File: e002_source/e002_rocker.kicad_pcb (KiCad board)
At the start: 2 copper layers, 32.2 x 75.2 mm, 48 parts, among them IC1 IC_TEXAS_TPS62743YFPR, IC2 DRV8317HREER, J1 USB_C_Receptacle_USB2.0_16P, U1 ESP32-S3-WROOM-1-N8R2

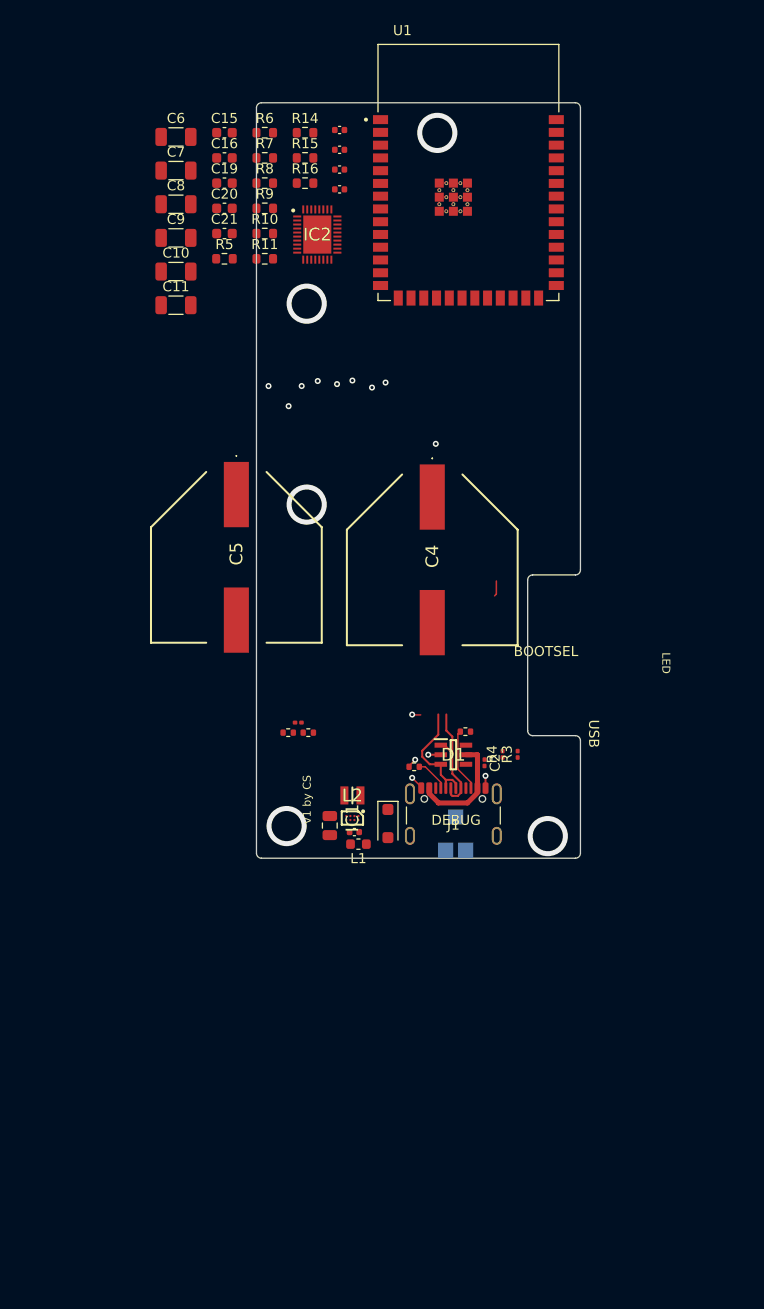
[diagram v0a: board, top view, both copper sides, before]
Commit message: removed STM MCU to optimize cost
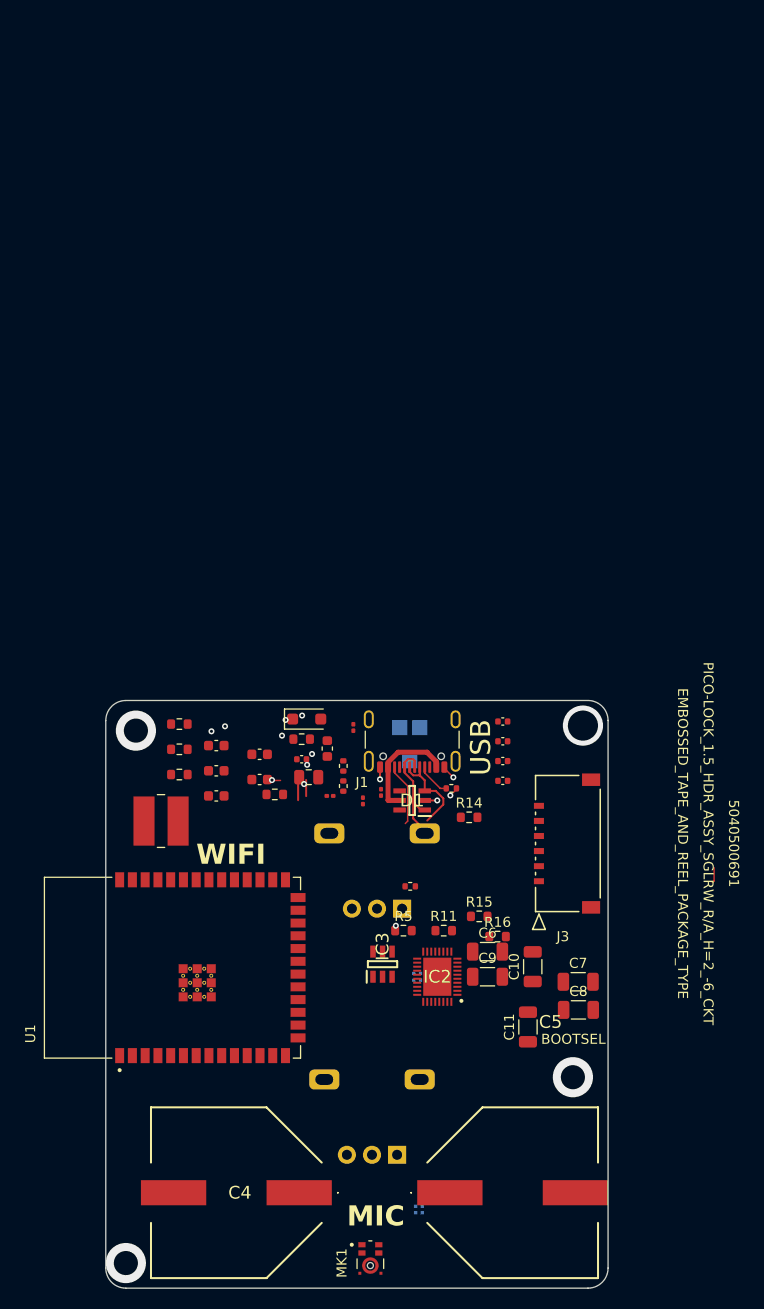
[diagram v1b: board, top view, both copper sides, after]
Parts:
- removed IC1: IC_TEXAS_TPS62743YFPR, smv_footprints:BGA8C40P2X4_87X156X53
- removed L2: 2.2u, smv_footprints:IND_MURATA_DFE201610P-2R2M=P2
- added IC3: ~, smv_footprints:SOT95P280X125-6N, F.Cu at (141.6, 127.8)
- added J3: 5040500691, smv_footprints:CONN_MOLEX_5040500691, F.Cu at (157.1, 119.5)
- added L3: INDC_TDK_VLCF5028T-220MR71-2, smv_footprints:IND_TDK_VLCF5028T-220MR71-2, F.Cu at (119.5, 113.5)
- added LED1: RGB, smv_footprints:DIOD_CREE_UHD111A-FKA-C3K23E1L3VG5ZB3Z3, B.Cu at (145.0, 129.0)
- added LED2: RGB, smv_footprints:DIOD_CREE_UHD111A-FKA-C3K23E1L3VG5ZB3Z3, B.Cu at (145.2, 152.2)
- added MK1: ~, smv_footprints:IC_MIC_TDK_MMICT5837-00-012, F.Cu at (140.3, 157.0)
- added RV1: R_Potentiometer, Potentiometer_THT:Potentiometer_Alps_RK09L_Single_Vertical, B.Cu at (143.0, 146.7)
- added RV1: R_Potentiometer, Potentiometer_THT:Potentiometer_Alps_RK09L_Single_Vertical, B.Cu at (143.5, 122.2)
- moved C7 90.1 mm to (161.0, 129.5)
- moved C8 89.7 mm to (161.1, 132.3)
- moved C6 86.8 mm to (152.0, 126.5)
- moved U1 84.5 mm to (120.6, 128.1), turned to 90 degrees
- moved C11 79.9 mm to (156.0, 134.0), turned to 90 degrees
- moved C9 79.8 mm to (152.0, 129.0)
- moved C10 77.8 mm to (156.5, 128.0), turned to 90 degrees
- moved R15 77.5 mm to (151.2, 123.0)
- moved R16 77.4 mm to (153.0, 125.0)
- moved IC2 74.8 mm to (147.0, 129.0), turned to 180 degrees
- moved R14 70.1 mm to (150.2, 113.1)
- moved R11 69.2 mm to (147.6, 124.4)
- moved R5 69.2 mm to (143.6, 124.4)
- moved C5 69.0 mm to (154.5, 150.5), turned to 0 degrees
- moved C15 66.0 mm to (125.0, 111.0)
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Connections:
- C19 pad 1: Net-(C19-Pad1) -> /ISENS_C
- C20 pad 1: Net-(C20-Pad1) -> /ISENS_B
- C21 pad 1: Net-(U1-IO6) -> /ISENS_A
- IC2 pad 21: unconnected-(IC2-AGND-Pad21) -> GND
- IC2 pad 34: /ISENS_C -> Net-(IC2-SOC)
- IC2 pad 35: /ISENS_B -> Net-(IC2-SOB)
- IC2 pad 36: /ISENS_A -> Net-(IC2-SOA)
- R11 pad 1: Net-(C19-Pad1) -> /ISENS_C
- R11 pad 2: /ISENS_B -> Net-(IC2-SOC)
- R14 pad 1: Net-(C20-Pad1) -> /ISENS_B
- R14 pad 2: /ISENS_B -> Net-(IC2-SOB)
- R16 pad 1: Net-(U1-IO6) -> /ISENS_A
- R16 pad 2: /ISENS_B -> Net-(IC2-SOA)
- U1 pad 6: Net-(U1-IO6) -> unconnected-(U1-IO6-Pad6)
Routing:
- net +3V3: track 1.56 -> 5.19 mm, vias 0 -> 2
- net USB_DM: track 11.2 -> 9.21 mm
- net USB_DP: track 11.7 -> 10.1 mm
- net GND: vias 11 -> 9
- net unconnected-(D2-K-Pad1): vias 0 -> 1
- net Net-(IC3-VIN): vias 0 -> 1
- net Net-(IC2-GAIN): vias 0 -> 1
- net Net-(IC2-CP): vias 0 -> 1
- net Net-(C4-+): vias 0 -> 1
- net (no net): vias 8 -> 2
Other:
- board size 32.2 x 75.2 mm -> 50 x 58.5 mm
- board text added: "MIC"
- board text added: "WIFI"
- board text removed: "DEBUG"
- board text removed: "LED"
- board text removed: "STM SWD GND SWC"
- board text removed: "v1 by CS"
